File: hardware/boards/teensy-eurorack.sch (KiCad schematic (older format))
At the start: 50 parts, among them J27 Conn_01x02, J28 Conn_02x08_Odd_Even, U2 AD5754BREZ, U3 AD5754BREZ, U4 Teensy4.1, U5 MCP1700-2502E, U6 AD7606BSTZ, U7 6N138

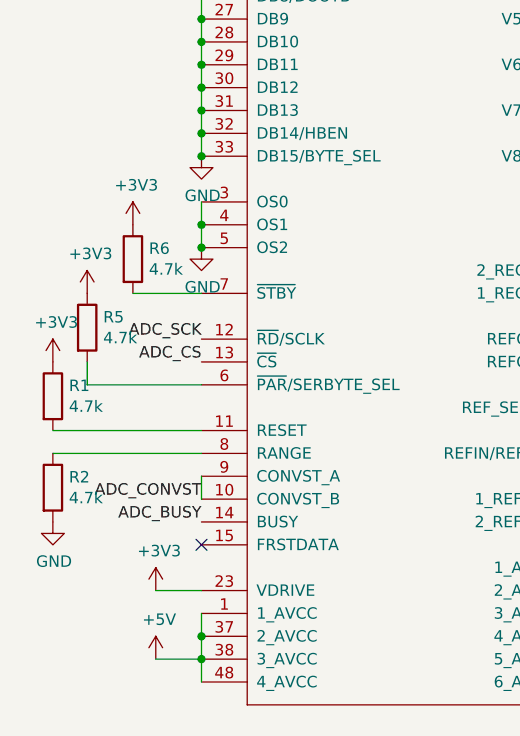
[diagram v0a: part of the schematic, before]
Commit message: schematic: fix ad7606 pin 8 (range select) from tied to gnd via res, to tied to 3v3 via resistor
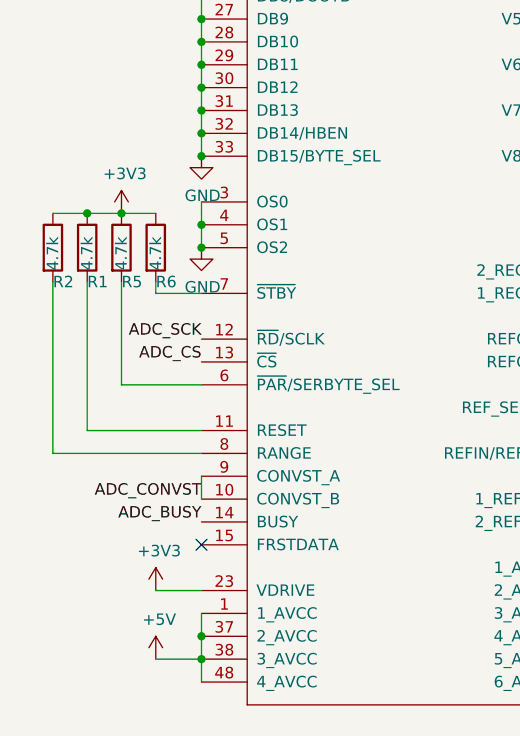
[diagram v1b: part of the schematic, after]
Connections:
- net +3V3: now also R2.1
- net GND: no longer R2.2
- net at U6.8 (RANGE): now also R2.2; no longer R2.1
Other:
- moved on the sheet: R1, R2, R5, R6
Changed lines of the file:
@@
 L Device:R R5
 U 1 1 5EE69443
-P 700 3500
-F 0 "R5" H 770 3546 50  0000 L CNN
-F 1 "4.7k" H 770 3455 50  0000 L CNN
-F 2 "Resistor_SMD:R_0805_2012Metric" V 630 3500 50  0001 C CNN
-F 3 "~" H 700 3500 50  0001 C CNN
-	1    700  3500
+P 850 3150
+F 0 "R5" H 850 3000 50  0000 L CNN
+F 1 "4.7k" V 850 3050 50  0000 L CNN
+F 2 "Resistor_SMD:R_0805_2012Metric" V 780 3150 50  0001 C CNN
+F 3 "~" H 850 3150 50  0001 C CNN
+	1    850  3150
 	1    0    0    -1
 $EndComp
@@
 L power:+3V3 #PWR073
 U 1 1 5EE6BD54
-P 700 3350
-F 0 "#PWR073" H 700 3200 50  0001 C CNN
-F 1 "+3V3" H 715 3523 50  0000 C CNN
-F 2 "" H 700 3350 50  0001 C CNN
-F 3 "" H 700 3350 50  0001 C CNN
-	1    700  3350
+P 850 3000
+F 0 "#PWR073" H 850 2850 50  0001 C CNN
+F 1 "+3V3" H 865 3173 50  0000 C CNN
+F 2 "" H 850 3000 50  0001 C CNN
+F 3 "" H 850 3000 50  0001 C CNN
+	1    850  3000
 	1    0    0    -1
 $EndComp
@@
 L Device:R R6
 U 1 1 5EE6DACC
-P 900 3200
-F 0 "R6" H 970 3246 50  0000 L CNN
-F 1 "4.7k" H 970 3155 50  0000 L CNN
-F 2 "Resistor_SMD:R_0805_2012Metric" V 830 3200 50  0001 C CNN
-F 3 "~" H 900 3200 50  0001 C CNN
-	1    900  3200
-	1    0    0    -1
-$EndComp
-Wire Wire Line
-	900  3350 1200 3350
-$Comp
-L power:+3V3 #PWR076
-U 1 1 5EE6FF2A
-P 900 3050
-F 0 "#PWR076" H 900 2900 50  0001 C CNN
-F 1 "+3V3" H 915 3223 50  0000 C CNN
-F 2 "" H 900 3050 50  0001 C CNN
-F 3 "" H 900 3050 50  0001 C CNN
-	1    900  3050
-	1    0    0    -1
-$EndComp
-$Comp
-L power:GND #PWR074
-U 1 1 5EE71FB6
-P 550 4350
-F 0 "#PWR074" H 550 4100 50  0001 C CNN
-F 1 "GND" H 555 4177 50  0000 C CNN
-F 2 "" H 550 4350 50  0001 C CNN
-F 3 "" H 550 4350 50  0001 C CNN
-	1    550  4350
-	1    0    0    -1
-$EndComp
+P 1000 3150
+F 0 "R6" H 1000 3000 50  0000 L CNN
+F 1 "4.7k" V 1000 3050 50  0000 L CNN
+F 2 "Resistor_SMD:R_0805_2012Metric" V 930 3150 50  0001 C CNN
+F 3 "~" H 1000 3150 50  0001 C CNN
+	1    1000 3150
+	1    0    0    -1
+$EndComp
+Wire Wire Line
+	1000 3350 1200 3350
 Wire Wire Line
 	550  4050 1200 4050
@@
 Wire Notes Line
 	7950 9550 8000 9550
-Wire Wire Line
-	550  3950 1200 3950
 Text Label 10200 5250 0    50   ~ 0
 DAC_REF2V5
@@
 	500  5550 7000 5550
 Wire Wire Line
-	700  3650 700  3750
-Wire Wire Line
-	700  3750 1200 3750
+	850  3300 850  3750
+Wire Wire Line
+	850  3750 1200 3750
 $Comp
 L Device:R R1
 U 1 1 5F517C04
-P 550 3800
-F 0 "R1" H 620 3846 50  0000 L CNN
-F 1 "4.7k" H 620 3755 50  0000 L CNN
-F 2 "Resistor_SMD:R_0805_2012Metric" V 480 3800 50  0001 C CNN
-F 3 "~" H 550 3800 50  0001 C CNN
-	1    550  3800
-	1    0    0    -1
-$EndComp
-$Comp
-L power:+3V3 #PWR01
-U 1 1 5F517C0A
-P 550 3650
-F 0 "#PWR01" H 550 3500 50  0001 C CNN
-F 1 "+3V3" H 565 3823 50  0000 C CNN
-F 2 "" H 550 3650 50  0001 C CNN
-F 3 "" H 550 3650 50  0001 C CNN
-	1    550  3650
+P 700 3150
+F 0 "R1" H 700 3000 50  0000 L CNN
+F 1 "4.7k" V 700 3050 50  0000 L CNN
+F 2 "Resistor_SMD:R_0805_2012Metric" V 630 3150 50  0001 C CNN
+F 3 "~" H 700 3150 50  0001 C CNN
+	1    700  3150
 	1    0    0    -1
 $EndComp
@@
 L Device:R R2
 U 1 1 5F5296C2
-P 550 4200
-F 0 "R2" H 620 4246 50  0000 L CNN
-F 1 "4.7k" H 620 4155 50  0000 L CNN
-F 2 "Resistor_SMD:R_0805_2012Metric" V 480 4200 50  0001 C CNN
-F 3 "~" H 550 4200 50  0001 C CNN
-	1    550  4200
+P 550 3150
+F 0 "R2" H 550 3000 50  0000 L CNN
+F 1 "4.7k" V 550 3050 50  0000 L CNN
+F 2 "Resistor_SMD:R_0805_2012Metric" V 480 3150 50  0001 C CNN
+F 3 "~" H 550 3150 50  0001 C CNN
+	1    550  3150
 	1    0    0    -1
 $EndComp
@@
 Wire Wire Line
 	6300 6000 6700 6000
+Wire Wire Line
+	1000 3350 1000 3300
+Wire Wire Line
+	1000 3000 850  3000
+Connection ~ 850  3000
+Wire Wire Line
+	700  3000 850  3000
+Wire Wire Line
+	550  3000 700  3000
+Connection ~ 700  3000
+Wire Wire Line
+	700  3300 700  3950
+Wire Wire Line
+	700  3950 1200 3950
+Wire Wire Line
+	550  3300 550  4050
 $EndSCHEMATC

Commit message: schematic: hookup ADC_RESET via pullup and ENC1A, ENC1B, ENC1SW
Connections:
- net ENC1A: now also U4.20 (28_RX7)
- net ENC1B: now also U4.21 (29_TX7)
- net ENC1SW: now also U4.22 (30_CRX3)
- net ADC_RESET: now reaches U4.6 (4_BCLK2)
- net ADC_RESET: now also R1.2, U6.11 (RESET)
- no-connect marks 41 -> 44
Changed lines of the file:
@@
 $EndDescr
-$Comp
-L teensy-eurorack:Teensy4.1_tht U4
-U 1 1 5ECE9695
-P 8800 3100
-F 0 "U4" H 8800 5665 50  0000 C CNN
-F 1 "Teensy4.1" H 8800 5574 50  0000 C CNN
-F 2 "footprints:Teensy41_tht" H 8400 3500 50  0001 C CNN
-F 3 "" H 8400 3500 50  0001 C CNN
-	1    8800 3100
-	1    0    0    -1
-$EndComp
 $Comp
 L power:GND #PWR044
@@
 NoConn ~ 7700 2450
 NoConn ~ 7700 2550
-NoConn ~ 7700 2850
-NoConn ~ 7700 2950
-NoConn ~ 7700 3050
-NoConn ~ 7700 1450
 $Comp
 L power:GND #PWR082
@@
 Wire Wire Line
 	850  3750 1200 3750
-$Comp
-L Device:R R1
-U 1 1 5F517C04
-P 700 3150
-F 0 "R1" H 700 3000 50  0000 L CNN
-F 1 "4.7k" V 700 3050 50  0000 L CNN
-F 2 "Resistor_SMD:R_0805_2012Metric" V 630 3150 50  0001 C CNN
-F 3 "~" H 700 3150 50  0001 C CNN
-	1    700  3150
-	1    0    0    -1
-$EndComp
 $Comp
 L Device:R R2
@@
 Connection ~ 850  3000
 Wire Wire Line
+	550  3300 550  4050
+Wire Wire Line
+	700  3950 1200 3950
+Wire Wire Line
+	700  3300 700  3950
+Wire Wire Line
+	550  3000 700  3000
+Wire Wire Line
 	700  3000 850  3000
-Wire Wire Line
-	550  3000 700  3000
 Connection ~ 700  3000
-Wire Wire Line
-	700  3300 700  3950
-Wire Wire Line
-	700  3950 1200 3950
-Wire Wire Line
-	550  3300 550  4050
+$Comp
+L Device:R R1
+U 1 1 5F517C04
+P 700 3150
+F 0 "R1" H 700 3000 50  0000 L CNN
+F 1 "4.7k" V 700 3050 50  0000 L CNN
+F 2 "Resistor_SMD:R_0805_2012Metric" V 630 3150 50  0001 C CNN
+F 3 "~" H 700 3150 50  0001 C CNN
+	1    700  3150
+	1    0    0    -1
+$EndComp
+Text Label 700  3950 0    49   ~ 0
+ADC_RESET
+$Comp
+L teensy-eurorack:Teensy4.1_tht U4
+U 1 1 5ECE9695
+P 8800 3100
+F 0 "U4" H 8800 5665 50  0000 C CNN
+F 1 "Teensy4.1" H 8800 5574 50  0000 C CNN
+F 2 "footprints:Teensy41_tht" H 8400 3500 50  0001 C CNN
+F 3 "" H 8400 3500 50  0001 C CNN
+	1    8800 3100
+	1    0    0    -1
+$EndComp
+Text Label 7700 1450 2    49   ~ 0
+ADC_RESET
+NoConn ~ 5750 6600
+NoConn ~ 5750 6700
+NoConn ~ 5750 6800
+NoConn ~ 5750 6900
+NoConn ~ 5800 7250
+NoConn ~ 5800 7350
+NoConn ~ 5800 7450
+Text Label 7700 2850 2    49   ~ 0
+ENC1A
+Text Label 7700 2950 2    49   ~ 0
+ENC1B
+Text Label 7700 3050 2    49   ~ 0
+ENC1SW
 $EndSCHEMATC
